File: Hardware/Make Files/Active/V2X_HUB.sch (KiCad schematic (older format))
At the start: 13 parts, among them U20 USB2242, X3 24MHz

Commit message: work from home day
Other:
- moved on the sheet: C55, C56, C57, C58, R77, R78, R79, R80, R81, R82, R83, U20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

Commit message: home to work push
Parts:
- added R18: DNS, Custom Parts:R_0603_sm, symbol R
- added R19, R60: 47K, Custom Parts:R_0603_sm, symbol R
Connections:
- net GND: now also R60.2
- net ~HUB_RESET: now also R18.2, R19.2, R60.1
- new net 5V0_HOST: R19.1
- new net HUB_ENABLE: R18.1
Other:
- note added: "Determines ~RESET~ control for HUB\nSet to Auto Host 5V0 detect"
- moved on the sheet: R81, R82, R83, X3
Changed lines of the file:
@@
 3V3_B
 $Comp
-L GND #PWR082
+L GND #PWR86
 U 1 1 55F890DF
 P 3450 2300
-F 0 "#PWR082" H 3450 2050 50  0001 C CNN
+F 0 "#PWR86" H 3450 2050 50  0001 C CNN
 F 1 "GND" V 3450 2100 50  0000 C CNN
 F 2 "" H 3450 2300 60  0000 C CNN
@@
 Text GLabel 4150 1250 2    60   Input ~ 0
 HUB_CLKN
-Text GLabel 3350 6450 2    60   Input ~ 0
+Text GLabel 6200 7150 2    60   Input ~ 0
 HUB_CLK
-Text GLabel 2650 6450 0    60   Input ~ 0
+Text GLabel 5500 7150 0    60   Input ~ 0
 HUB_CLKN
 Wire Wire Line
-	2650 6450 2800 6450
-Wire Wire Line
-	3200 6450 3350 6450
-$Comp
-L GND #PWR083
+	5500 7150 5650 7150
+Wire Wire Line
+	6050 7150 6200 7150
+$Comp
+L GND #PWR90
 U 1 1 55F89454
-P 3000 6550
-F 0 "#PWR083" H 3000 6300 50  0001 C CNN
-F 1 "GND" V 3000 6350 50  0000 C CNN
-F 2 "" H 3000 6550 60  0000 C CNN
-F 3 "" H 3000 6550 60  0000 C CNN
-	1    3000 6550
+P 5850 7250
+F 0 "#PWR90" H 5850 7000 50  0001 C CNN
+F 1 "GND" V 5850 7050 50  0000 C CNN
+F 2 "" H 5850 7250 60  0000 C CNN
+F 3 "" H 5850 7250 60  0000 C CNN
+	1    5850 7250
 	1    0    0    -1
 $EndComp
@@
 L R R81
 U 1 1 55F8A6E8
-P 3750 5100
-F 0 "R81" V 3830 5100 50  0000 C CNN
-F 1 "DNS" V 3750 5100 50  0000 C CNN
-F 2 "Custom Parts:R_0603_sm" V 3680 5100 30  0001 C CNN
-F 3 "" H 3750 5100 30  0000 C CNN
-	1    3750 5100
+P 7300 3450
+F 0 "R81" V 7380 3450 50  0000 C CNN
+F 1 "DNS" V 7300 3450 50  0000 C CNN
+F 2 "Custom Parts:R_0603_sm" V 7230 3450 30  0001 C CNN
+F 3 "" H 7300 3450 30  0000 C CNN
+	1    7300 3450
 	-1   0    0    1
 $EndComp
@@
 L R R83
 U 1 1 55F8A750
-P 3750 5600
-F 0 "R83" V 3830 5600 50  0000 C CNN
-F 1 "1K0" V 3750 5600 50  0000 C CNN
-F 2 "Custom Parts:R_0603_sm" V 3680 5600 30  0001 C CNN
-F 3 "http://www.vishay.com/doc?20035" H 3750 5600 30  0001 C CNN
-F 4 "71-CRCW0603-1.0K-E3" H 3750 5600 60  0001 C CNN "Mouse PN"
-	1    3750 5600
+P 7300 3950
+F 0 "R83" V 7380 3950 50  0000 C CNN
+F 1 "1K0" V 7300 3950 50  0000 C CNN
+F 2 "Custom Parts:R_0603_sm" V 7230 3950 30  0001 C CNN
+F 3 "http://www.vishay.com/doc?20035" H 7300 3950 30  0001 C CNN
+F 4 "71-CRCW0603-1.0K-E3" H 7300 3950 60  0001 C CNN "Mouse PN"
+	1    7300 3950
 	-1   0    0    1
 $EndComp
 Wire Wire Line
-	3750 5250 3750 5450
-Connection ~ 3750 5350
-Text GLabel 3650 4850 0    60   Input ~ 0
+	7300 3600 7300 3800
+Connection ~ 7300 3700
+Text GLabel 7200 3200 0    60   Input ~ 0
 3V3_B
 $Comp
-L GND #PWR084
+L GND #PWR91
 U 1 1 55F8A8AD
-P 3750 5750
-F 0 "#PWR084" H 3750 5500 50  0001 C CNN
-F 1 "GND" V 3750 5550 50  0000 C CNN
-F 2 "" H 3750 5750 60  0000 C CNN
-F 3 "" H 3750 5750 60  0000 C CNN
-	1    3750 5750
-	1    0    0    -1
-$EndComp
-Wire Wire Line
-	3750 4950 3750 4850
-Wire Wire Line
-	3750 4850 3650 4850
-Text Notes 1900 5300 0    60   ~ 0
+P 7300 4100
+F 0 "#PWR91" H 7300 3850 50  0001 C CNN
+F 1 "GND" V 7300 3900 50  0000 C CNN
+F 2 "" H 7300 4100 60  0000 C CNN
+F 3 "" H 7300 4100 60  0000 C CNN
+	1    7300 4100
+	1    0    0    -1
+$EndComp
+Wire Wire Line
+	7300 3300 7300 3200
+Wire Wire Line
+	7300 3200 7200 3200
+Text Notes 5450 3650 0    60   ~ 0
 Boot Strapping Option\nPRTPWR1 = Battery Charge Enable\n0  = feature off, we dont need.
 $Comp
-L GND #PWR085
+L GND #PWR89
 U 1 1 55F8AB65
 P 5100 950
-F 0 "#PWR085" H 5100 700 50  0001 C CNN
+F 0 "#PWR89" H 5100 700 50  0001 C CNN
 F 1 "GND" V 5100 750 50  0000 C CNN
 F 2 "" H 5100 950 60  0000 C CNN
@@
 Connection ~ 1250 1750
 $Comp
-L GND #PWR086
+L GND #PWR83
 U 1 1 55F8AFDA
 P 1250 2050
-F 0 "#PWR086" H 1250 1800 50  0001 C CNN
+F 0 "#PWR83" H 1250 1800 50  0001 C CNN
 F 1 "GND" V 1250 1850 50  0000 C CNN
 F 2 "" H 1250 2050 60  0000 C CNN
@@
 Connection ~ 1750 950
 $Comp
-L GND #PWR087
+L GND #PWR85
 U 1 1 55F8B30B
 P 1750 1250
-F 0 "#PWR087" H 1750 1000 50  0001 C CNN
+F 0 "#PWR85" H 1750 1000 50  0001 C CNN
 F 1 "GND" V 1750 1050 50  0000 C CNN
 F 2 "" H 1750 1250 60  0000 C CNN
@@
 	1600 1850 2750 1850
 $Comp
-L GND #PWR088
+L GND #PWR84
 U 1 1 55F8B452
 P 1600 2300
-F 0 "#PWR088" H 1600 2050 50  0001 C CNN
+F 0 "#PWR84" H 1600 2050 50  0001 C CNN
 F 1 "GND" V 1600 2100 50  0000 C CNN
 F 2 "" H 1600 2300 60  0000 C CNN
@@
 	4150 1050 4800 1050
 $Comp
-L GND #PWR089
+L GND #PWR88
 U 1 1 55F8B6A0
 P 4800 1350
-F 0 "#PWR089" H 4800 1100 50  0001 C CNN
+F 0 "#PWR88" H 4800 1100 50  0001 C CNN
 F 1 "GND" V 4800 1150 50  0000 C CNN
 F 2 "" H 4800 1350 60  0000 C CNN
@@
 	1    0    0    -1
 $EndComp
-Text Notes 1950 5700 0    60   ~ 0
+Text Notes 5500 4050 0    60   ~ 0
 PRTPWR1 and PRTPWR2 go\n high when the port is active
 Text GLabel 4150 1750 2    60   Input ~ 0
 3V3_B
 Wire Wire Line
-	3650 5400 3750 5400
-Connection ~ 3750 5400
+	7200 3750 7300 3750
+Connection ~ 7300 3750
 Text GLabel 4150 1950 2    60   Input ~ 0
 HUB_SCL
@@
 HUB_SDA
 $Comp
-L GND #PWR090
+L GND #PWR87
 U 1 1 55F9C2E3
 P 3700 4250
-F 0 "#PWR090" H 3700 4000 50  0001 C CNN
+F 0 "#PWR87" H 3700 4000 50  0001 C CNN
 F 1 "GND" V 3700 4050 50  0000 C CNN
 F 2 "" H 3700 4250 60  0000 C CNN
@@
 Text GLabel 2750 1550 0    69   Input ~ 0
 HUB_PWR_PRT1
-Text GLabel 4150 5350 2    69   Input ~ 0
+Text GLabel 7700 3700 2    69   Input ~ 0
 HUB_STATUS
 Text GLabel 4150 3850 2    69   Input ~ 0
@@
 Wire Wire Line
 	3850 3850 3700 3850
-Text GLabel 3650 5400 0    69   Input ~ 0
+Text GLabel 7200 3750 0    69   Input ~ 0
 HUB_PWR_PRT1
 Wire Wire Line
-	3750 5350 3850 5350
+	7300 3700 7400 3700
 Text GLabel 4150 1550 2    60   Input ~ 0
 3V3_B
@@
 L R R82
 U 1 1 56070A80
-P 4000 5350
-F 0 "R82" V 4080 5350 50  0000 C CNN
-F 1 "1K0" V 4000 5350 50  0000 C CNN
-F 2 "Custom Parts:R_0603_sm" V 3930 5350 30  0001 C CNN
-F 3 "http://www.vishay.com/doc?20035" H 4000 5350 30  0001 C CNN
-F 4 "71-CRCW0603-1.0K-E3" H 4000 5350 60  0001 C CNN "Mouse PN"
-	1    4000 5350
+P 7550 3700
+F 0 "R82" V 7630 3700 50  0000 C CNN
+F 1 "1K0" V 7550 3700 50  0000 C CNN
+F 2 "Custom Parts:R_0603_sm" V 7480 3700 30  0001 C CNN
+F 3 "http://www.vishay.com/doc?20035" H 7550 3700 30  0001 C CNN
+F 4 "71-CRCW0603-1.0K-E3" H 7550 3700 60  0001 C CNN "Mouse PN"
+	1    7550 3700
 	0    -1   -1   0
 $EndComp
@@
 L CRYSTAL_SMD X3
 U 1 1 56092E15
-P 3000 6450
-F 0 "X3" H 3000 6540 50  0000 C CNN
-F 1 "24MHz" H 3030 6340 50  0000 L CNN
-F 2 "Custom Parts:AWSCR" H 3000 6450 60  0001 C CNN
-F 3 "http://www.abracon.com/Resonators/N_AWSCR-MT.pdf" H 3000 6450 60  0001 C CNN
-F 4 "815-AWSCR-24.00MTD-T" H 3000 6450 60  0001 C CNN "Mouse PN"
-	1    3000 6450
-	1    0    0    -1
+P 5850 7150
+F 0 "X3" H 5850 7240 50  0000 C CNN
+F 1 "24MHz" H 5880 7040 50  0000 L CNN
+F 2 "Custom Parts:AWSCR" H 5850 7150 60  0001 C CNN
+F 3 "http://www.abracon.com/Resonators/N_AWSCR-MT.pdf" H 5850 7150 60  0001 C CNN
+F 4 "815-AWSCR-24.00MTD-T" H 5850 7150 60  0001 C CNN "Mouse PN"
+	1    5850 7150
+	1    0    0    -1
+$EndComp
+Text GLabel 7500 1000 2    60   Input ~ 0
+~HUB_RESET
+Text GLabel 6900 1200 0    60   Input ~ 0
+5V0_HOST
+Text GLabel 6900 1000 0    60   Input ~ 0
+HUB_ENABLE
+$Comp
+L R R18
+U 1 1 5627870C
+P 7150 1000
+F 0 "R18" V 7230 1000 50  0000 C CNN
+F 1 "DNS" V 7150 1000 50  0000 C CNN
+F 2 "Custom Parts:R_0603_sm" V 7080 1000 30  0001 C CNN
+F 3 "" H 7150 1000 30  0000 C CNN
+	1    7150 1000
+	0    -1   -1   0
+$EndComp
+Wire Wire Line
+	7300 1000 7500 1000
+Wire Wire Line
+	7400 1000 7400 1200
+Wire Wire Line
+	7300 1200 7500 1200
+Connection ~ 7400 1000
+Wire Wire Line
+	7000 1000 6900 1000
+Wire Wire Line
+	6900 1200 7000 1200
+Text Notes 6200 1500 0    69   ~ 0
+Determines ~RESET~ control for HUB\nSet to Auto Host 5V0 detect
+$Comp
+L R R19
+U 1 1 5627871B
+P 7150 1200
+F 0 "R19" V 7230 1200 50  0000 C CNN
+F 1 "47K" V 7150 1200 50  0000 C CNN
+F 2 "Custom Parts:R_0603_sm" V 7080 1200 30  0001 C CNN
+F 3 "http://www.mouser.com/ds/2/427/dcrcwe3-109170.pdf" H 7150 1200 30  0001 C CNN
+F 4 "71-CRCW0603-47K-E3" H 7150 1200 60  0001 C CNN "Mouse PN"
+	1    7150 1200
+	0    -1   -1   0
+$EndComp
+$Comp
+L R R60
+U 1 1 56278723
+P 7650 1200
+F 0 "R60" V 7730 1200 50  0000 C CNN
+F 1 "47K" V 7650 1200 50  0000 C CNN
+F 2 "Custom Parts:R_0603_sm" V 7580 1200 30  0001 C CNN
+F 3 "http://www.mouser.com/ds/2/427/dcrcwe3-109170.pdf" H 7650 1200 30  0001 C CNN
+F 4 "71-CRCW0603-47K-E3" H 7650 1200 60  0001 C CNN "Mouse PN"
+	1    7650 1200
+	0    -1   -1   0
+$EndComp
+Connection ~ 7400 1200
+$Comp
+L GND #PWR92
+U 1 1 5627872B
+P 7800 1200
+F 0 "#PWR92" H 7800 950 50  0001 C CNN
+F 1 "GND" V 7800 1000 50  0000 C CNN
+F 2 "" H 7800 1200 60  0000 C CNN
+F 3 "" H 7800 1200 60  0000 C CNN
+	1    7800 1200
+	0    -1   -1   0
 $EndComp
 $EndSCHEMATC

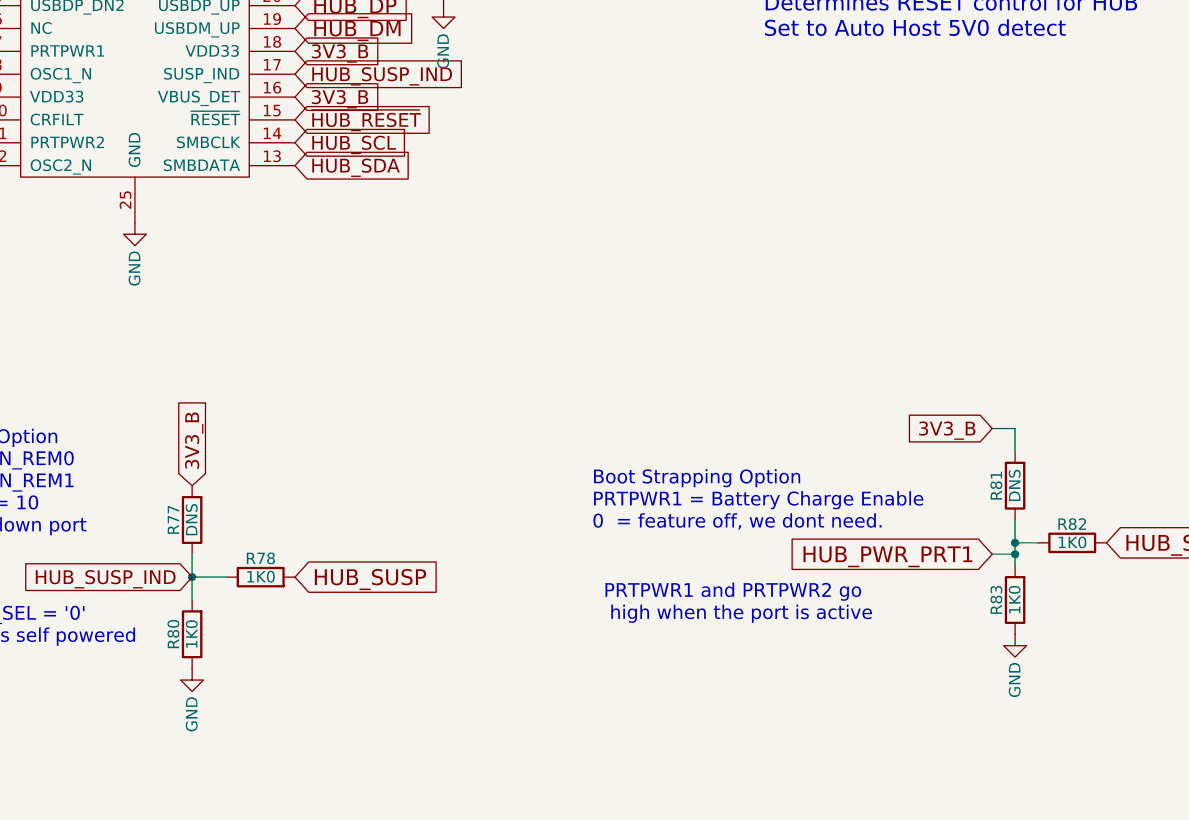
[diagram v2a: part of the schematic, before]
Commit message: Verification findings and modifications
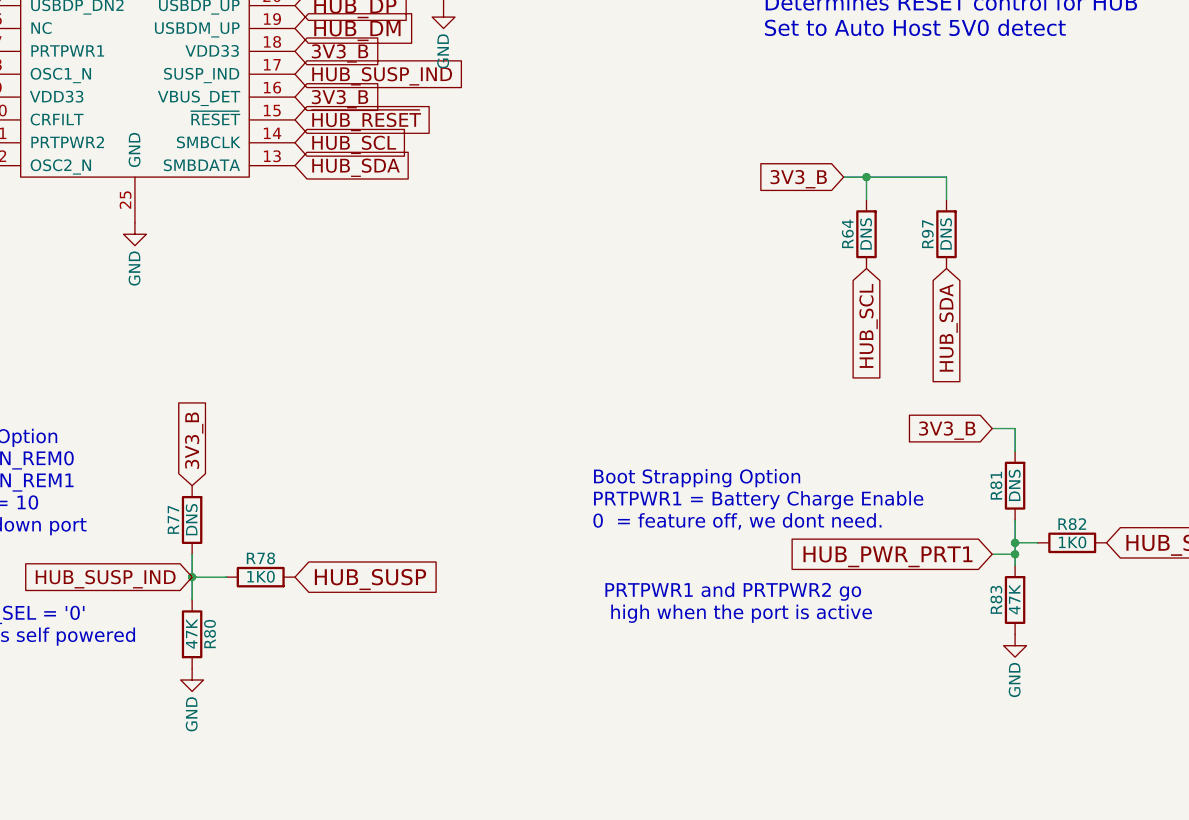
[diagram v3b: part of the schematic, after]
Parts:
- added R64, R97: DNS, Custom Parts:R_0603_sm, symbol R
- R80, R83: value 1K0 -> 47K; Mouse PN 71-CRCW0603-1.0K-E3 -> 71-CRCW0603-47K-E3
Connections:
- net 3V3_B: now also R64.2, R97.2
- net GND: now also R80.2; no longer R80.1
- net HUB_SCL: now also R64.1
- net HUB_SDA: now also R97.1
- net HUB_SUSP_IND: now also R80.1; no longer R80.2
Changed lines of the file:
@@
 3V3_B
 $Comp
-L GND #PWR86
+L GND #PWR082
 U 1 1 55F890DF
 P 3450 2300
-F 0 "#PWR86" H 3450 2050 50  0001 C CNN
+F 0 "#PWR082" H 3450 2050 50  0001 C CNN
 F 1 "GND" V 3450 2100 50  0000 C CNN
 F 2 "" H 3450 2300 60  0000 C CNN
@@
 	6050 7150 6200 7150
 $Comp
-L GND #PWR90
+L GND #PWR083
 U 1 1 55F89454
 P 5850 7250
-F 0 "#PWR90" H 5850 7000 50  0001 C CNN
+F 0 "#PWR083" H 5850 7000 50  0001 C CNN
 F 1 "GND" V 5850 7050 50  0000 C CNN
 F 2 "" H 5850 7250 60  0000 C CNN
@@
 	-1   0    0    1
 $EndComp
-$Comp
-L R R83
-U 1 1 55F8A750
-P 7300 3950
-F 0 "R83" V 7380 3950 50  0000 C CNN
-F 1 "1K0" V 7300 3950 50  0000 C CNN
-F 2 "Custom Parts:R_0603_sm" V 7230 3950 30  0001 C CNN
-F 3 "http://www.vishay.com/doc?20035" H 7300 3950 30  0001 C CNN
-F 4 "71-CRCW0603-1.0K-E3" H 7300 3950 60  0001 C CNN "Mouse PN"
-	1    7300 3950
-	-1   0    0    1
-$EndComp
 Wire Wire Line
 	7300 3600 7300 3800
@@
 3V3_B
 $Comp
-L GND #PWR91
+L GND #PWR084
 U 1 1 55F8A8AD
 P 7300 4100
-F 0 "#PWR91" H 7300 3850 50  0001 C CNN
+F 0 "#PWR084" H 7300 3850 50  0001 C CNN
 F 1 "GND" V 7300 3900 50  0000 C CNN
 F 2 "" H 7300 4100 60  0000 C CNN
@@
 Boot Strapping Option\nPRTPWR1 = Battery Charge Enable\n0  = feature off, we dont need.
 $Comp
-L GND #PWR89
+L GND #PWR085
 U 1 1 55F8AB65
 P 5100 950
-F 0 "#PWR89" H 5100 700 50  0001 C CNN
+F 0 "#PWR085" H 5100 700 50  0001 C CNN
 F 1 "GND" V 5100 750 50  0000 C CNN
 F 2 "" H 5100 950 60  0000 C CNN
@@
 Connection ~ 1250 1750
 $Comp
-L GND #PWR83
+L GND #PWR086
 U 1 1 55F8AFDA
 P 1250 2050
-F 0 "#PWR83" H 1250 1800 50  0001 C CNN
+F 0 "#PWR086" H 1250 1800 50  0001 C CNN
 F 1 "GND" V 1250 1850 50  0000 C CNN
 F 2 "" H 1250 2050 60  0000 C CNN
@@
 Connection ~ 1750 950
 $Comp
-L GND #PWR85
+L GND #PWR087
 U 1 1 55F8B30B
 P 1750 1250
-F 0 "#PWR85" H 1750 1000 50  0001 C CNN
+F 0 "#PWR087" H 1750 1000 50  0001 C CNN
 F 1 "GND" V 1750 1050 50  0000 C CNN
 F 2 "" H 1750 1250 60  0000 C CNN
@@
 	1600 1850 2750 1850
 $Comp
-L GND #PWR84
+L GND #PWR088
 U 1 1 55F8B452
 P 1600 2300
-F 0 "#PWR84" H 1600 2050 50  0001 C CNN
+F 0 "#PWR088" H 1600 2050 50  0001 C CNN
 F 1 "GND" V 1600 2100 50  0000 C CNN
 F 2 "" H 1600 2300 60  0000 C CNN
@@
 	4150 1050 4800 1050
 $Comp
-L GND #PWR88
+L GND #PWR089
 U 1 1 55F8B6A0
 P 4800 1350
-F 0 "#PWR88" H 4800 1100 50  0001 C CNN
+F 0 "#PWR089" H 4800 1100 50  0001 C CNN
 F 1 "GND" V 4800 1150 50  0000 C CNN
 F 2 "" H 4800 1350 60  0000 C CNN
@@
 HUB_SDA
 $Comp
-L GND #PWR87
+L GND #PWR090
 U 1 1 55F9C2E3
 P 3700 4250
-F 0 "#PWR87" H 3700 4000 50  0001 C CNN
+F 0 "#PWR090" H 3700 4000 50  0001 C CNN
 F 1 "GND" V 3700 4050 50  0000 C CNN
 F 2 "" H 3700 4250 60  0000 C CNN
@@
 $EndComp
 $Comp
-L R R80
-U 1 1 5607098B
-P 3700 4100
-F 0 "R80" V 3780 4100 50  0000 C CNN
-F 1 "1K0" V 3700 4100 50  0000 C CNN
-F 2 "Custom Parts:R_0603_sm" V 3630 4100 30  0001 C CNN
-F 3 "http://www.vishay.com/doc?20035" H 3700 4100 30  0001 C CNN
-F 4 "71-CRCW0603-1.0K-E3" H 3700 4100 60  0001 C CNN "Mouse PN"
-	1    3700 4100
-	-1   0    0    1
-$EndComp
-$Comp
 L R R78
 U 1 1 56070A28
@@
 Connection ~ 7400 1200
 $Comp
-L GND #PWR92
+L GND #PWR091
 U 1 1 5627872B
 P 7800 1200
-F 0 "#PWR92" H 7800 950 50  0001 C CNN
+F 0 "#PWR091" H 7800 950 50  0001 C CNN
 F 1 "GND" V 7800 1000 50  0000 C CNN
 F 2 "" H 7800 1200 60  0000 C CNN
@@
 	0    -1   -1   0
 $EndComp
+$Comp
+L R R80
+U 1 1 5627F427
+P 3700 4100
+F 0 "R80" V 3780 4100 50  0000 C CNN
+F 1 "47K" V 3700 4100 50  0000 C CNN
+F 2 "Custom Parts:R_0603_sm" V 3630 4100 30  0001 C CNN
+F 3 "http://www.mouser.com/ds/2/427/dcrcwe3-109170.pdf" H 3700 4100 30  0001 C CNN
+F 4 "71-CRCW0603-47K-E3" H 3700 4100 60  0001 C CNN "Mouse PN"
+	1    3700 4100
+	1    0    0    -1
+$EndComp
+$Comp
+L R R83
+U 1 1 5627F762
+P 7300 3950
+F 0 "R83" V 7380 3950 50  0000 C CNN
+F 1 "47K" V 7300 3950 50  0000 C CNN
+F 2 "Custom Parts:R_0603_sm" V 7230 3950 30  0001 C CNN
+F 3 "http://www.mouser.com/ds/2/427/dcrcwe3-109170.pdf" H 7300 3950 30  0001 C CNN
+F 4 "71-CRCW0603-47K-E3" H 7300 3950 60  0001 C CNN "Mouse PN"
+	1    7300 3950
+	-1   0    0    1
+$EndComp
+$Comp
+L R R64
+U 1 1 56280338
+P 6650 2350
+F 0 "R64" V 6730 2350 50  0000 C CNN
+F 1 "DNS" V 6650 2350 50  0000 C CNN
+F 2 "Custom Parts:R_0603_sm" V 6580 2350 30  0001 C CNN
+F 3 "" H 6650 2350 30  0000 C CNN
+	1    6650 2350
+	-1   0    0    1
+$EndComp
+Text GLabel 6550 2100 0    60   Input ~ 0
+3V3_B
+Wire Wire Line
+	6650 2200 6650 2100
+Wire Wire Line
+	6550 2100 7000 2100
+Text GLabel 6650 2500 3    60   Input ~ 0
+HUB_SCL
+$Comp
+L R R97
+U 1 1 56280403
+P 7000 2350
+F 0 "R97" V 7080 2350 50  0000 C CNN
+F 1 "DNS" V 7000 2350 50  0000 C CNN
+F 2 "Custom Parts:R_0603_sm" V 6930 2350 30  0001 C CNN
+F 3 "" H 7000 2350 30  0000 C CNN
+	1    7000 2350
+	-1   0    0    1
+$EndComp
+Wire Wire Line
+	7000 2100 7000 2200
+Text GLabel 7000 2500 3    60   Input ~ 0
+HUB_SDA
+Connection ~ 6650 2100
 $EndSCHEMATC

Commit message: BOM updates
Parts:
- R78, R82: value 1K0 -> 1K
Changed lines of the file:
@@
 P 4000 3850
 F 0 "R78" V 4080 3850 50  0000 C CNN
-F 1 "1K0" V 4000 3850 50  0000 C CNN
+F 1 "1K" V 4000 3850 50  0000 C CNN
 F 2 "Custom Parts:R_0603_sm" V 3930 3850 30  0001 C CNN
 F 3 "http://www.vishay.com/doc?20035" H 4000 3850 30  0001 C CNN
@@
 P 7550 3700
 F 0 "R82" V 7630 3700 50  0000 C CNN
-F 1 "1K0" V 7550 3700 50  0000 C CNN
+F 1 "1K" V 7550 3700 50  0000 C CNN
 F 2 "Custom Parts:R_0603_sm" V 7480 3700 30  0001 C CNN
 F 3 "http://www.vishay.com/doc?20035" H 7550 3700 30  0001 C CNN

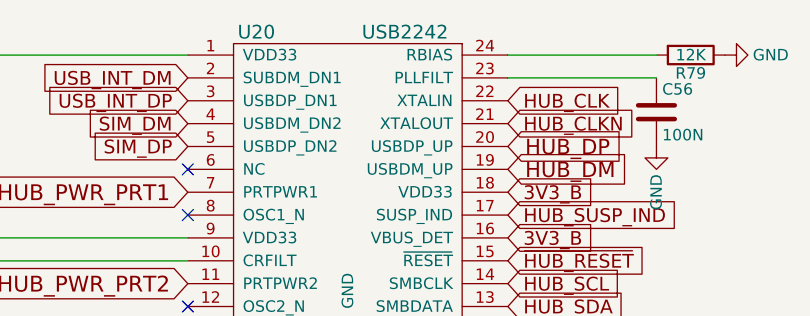
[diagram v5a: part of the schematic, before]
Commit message: Added learnings from V1.2 build
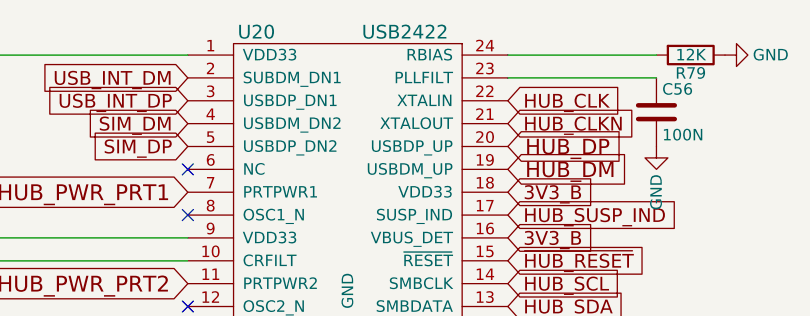
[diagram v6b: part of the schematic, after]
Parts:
- U20: value USB2242 -> USB2422
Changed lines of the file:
@@
 P 3450 1500
 F 0 "U20" H 3050 2150 60  0000 C CNN
-F 1 "USB2242" H 3700 2150 60  0000 C CNN
+F 1 "USB2422" H 3700 2150 60  0000 C CNN
 F 2 "Housings_DFN_QFN:QFN-24-1EP_4x4mm_Pitch0.5mm" H 3450 1500 60  0001 C CNN
 F 3 "http://www.mouser.com/ds/2/268/2422-319423.pdf" H 3450 1500 60  0001 C CNN

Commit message: 53534 New design verified
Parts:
- removed R18, R64, R77, R81, R97: DNS, Custom Parts:R_0603_sm, symbol R
- removed R78, R82: 1K, Custom Parts:R_0603_sm, symbol R
- added C?: 4U7, Custom Parts:C_0805_SM, symbol C
- added C?: 100N, Custom Parts:C_0603_SM, symbol C
- added FB?: 220, Custom Parts:R_0603_sm, symbol FILTER
- added P?: USB_u, Custom Parts:USB_Micro-B-DX4R005JJ2R1800, symbol USB_OTG
- added R? (x2): 47K, Custom Parts:R_0603_sm, symbol R
- added U?: ADXL345, Custom Parts:LGA-14_5x3mm, symbol ADXL345
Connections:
- net 3V3_B: now also R?.2
- net 5V0_HOST: now also P?.1 (VCC)
- net GND: now also R80.1, R83.2, C?.2, C?.2, P?.5 (GND), P?.6 (shield), R?.2, U?.2 (GND), U?.4 (GND), U?.5 (GND); no longer R80.2, R83.1
- net HUB_DM: now also P?.2 (D-)
- net HUB_DP: now also P?.3 (D+)
- net HUB_PWR_PRT1: now also R83.1; no longer R83.2
- net HUB_SCL: now also R?.1
- net HUB_SDA: now also R?.1
- net HUB_SUSP_IND: now also R80.2; no longer R80.1
- new net: C?.1, FB?.2, U?.6 (VS)
- new net 3V3_D: C?.1, FB?.1, U?.1 (V_IO)
- new net ACL_INT1: U?.8 (INT1)
- new net ACL_INT2: U?.9 (INT2)
- new net SEQ_MISO: U?.12 (SDO/ALT)
- new net SEQ_MOSI: U?.13 (SDA/SDI)
- new net SEQ_SCK: U?.14 (SCL/SCK)
- new net SEQ_SS: U?.7 (CS)
- no-connect marks 3 -> 4
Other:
- note added: "(NON_REM0)"
- note added: "(NON_REM1)"
- note added: "0: Battery charging feature is not supported for port 1"
- note added: "0: Default configuration: Strap options enabled, hub as “self-powered”"
- note added: "Bootstrapping Options"
- note added: "HUB Data"
- note added: "NON_REM[1:0] = 10: ports 1 and 2 are non-removable"
- note removed: "Boot Strapping Option\nPRTPWR1 = Battery Charge Enable\n0 = feature off, we dont need."
- note removed: "Boot Strapping Option\nSUSP_IND = NON_REM0\nSMBDATA = NON_REM1\nNON_REM[1:0] = 10 \nmeans neither down port\n is removable \n\n\nSMBCLK = CFG_SEL = '0'\nMeans the hub is self powered"
- note removed: "PRTPWR1 and PRTPWR2 go\n high when the port is active"
- moved on the sheet: R19, R60, R80, R83, X3
